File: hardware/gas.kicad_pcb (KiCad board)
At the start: 2 copper layers, 65 x 30 mm, 24 parts, among them P1 CON-SENSOR2, P2 DEBUG, P3 BOOT, P4 Gas Sensor, U1 XMC1300, U2 DRILL, U3 DRILL, U4 DRILL, U5 DRILL

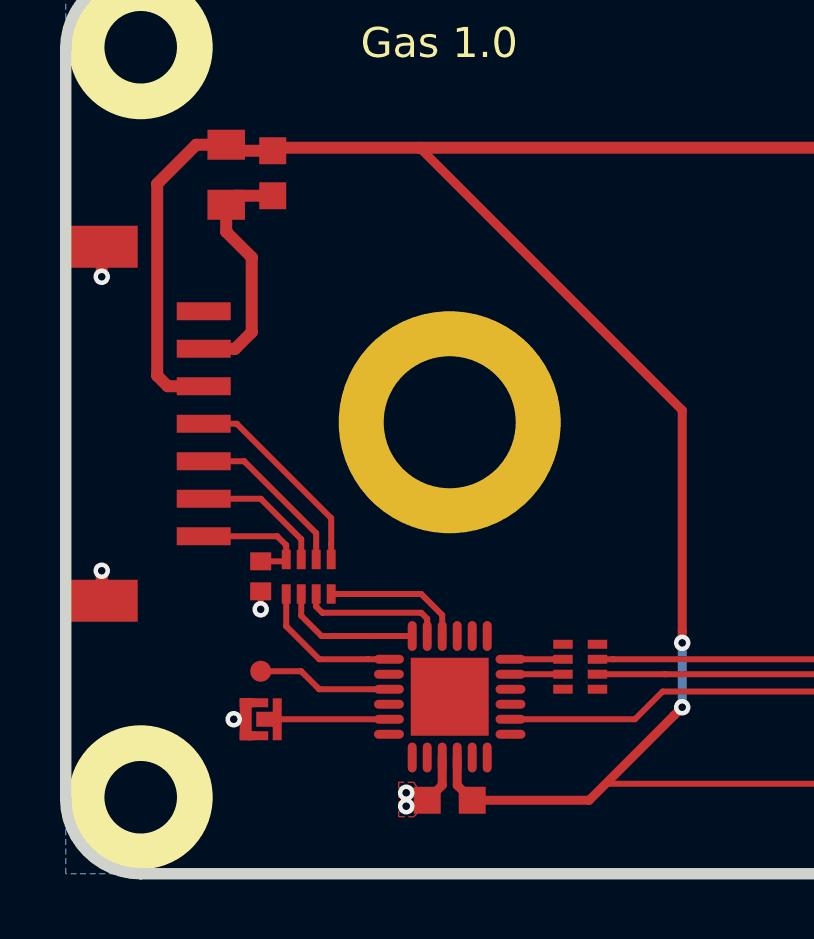
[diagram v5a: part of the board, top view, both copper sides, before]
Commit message: updated M3 spacer footprint, drc check
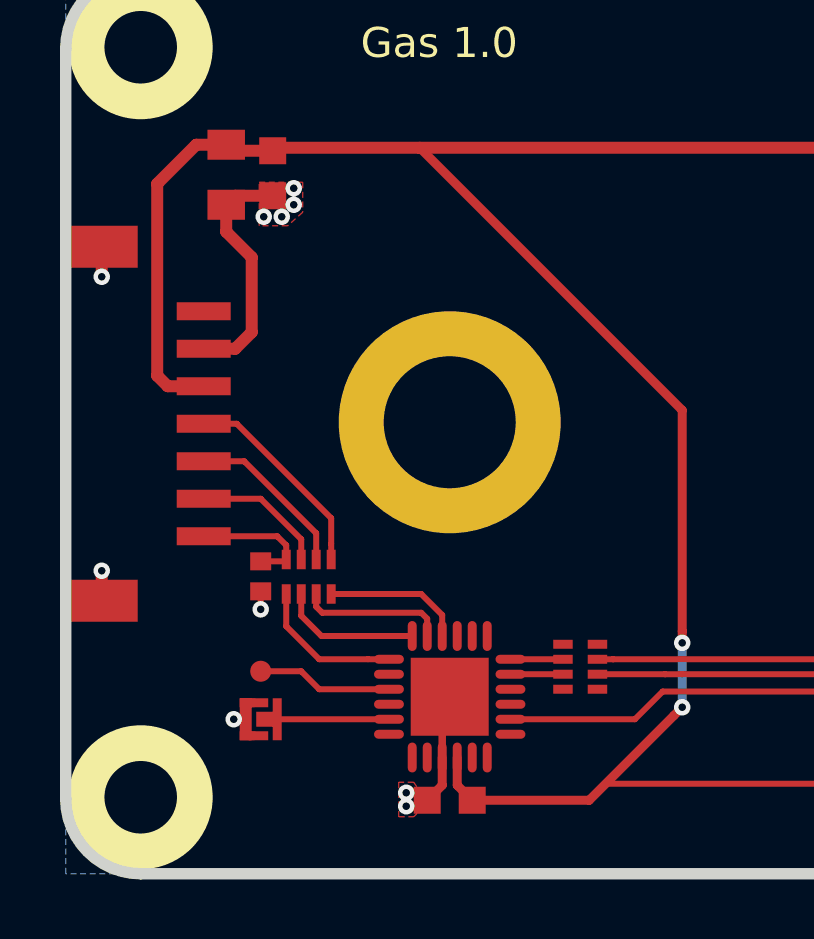
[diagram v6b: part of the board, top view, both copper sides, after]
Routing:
- net GND: track 25.9 -> 31.4 mm, vias 8 -> 12
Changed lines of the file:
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@@
-(kicad_pcb (version 20171130) (host pcbnew 5.0.2-bee76a0~70~ubuntu18.04.1)
+(kicad_pcb (version 20171130) (host pcbnew 5.0.2-bee76a0~70~ubuntu18.10.1)
   (general
     (thickness 1.6)
     (drawings 15)
-    (tracks 137)
+    (tracks 146)
     (zones 0)
     (modules 24)
@@
   )
   (setup
-    (last_trace_width 0.2)
+    (last_trace_width 0.4)
     (user_trace_width 0.2)
     (user_trace_width 0.3)
@@
       (effects (font (size 0.3 0.3) (thickness 0.05)))
     )
-    (pad "" thru_hole circle (at 0 0) (size 7.4 7.4) (drill 4.4) (layers *.Cu *.Mask F.Paste))
+    (fp_poly (pts (xy 2.12 0.61) (xy 2.23 0.15) (xy 3.71 0.15) (xy 3.54 1.08)) (layer F.Paste) (width 0))
+    (fp_poly (pts (xy -0.665 2.11) (xy -0.15 2.2) (xy -0.15 3.68) (xy -1.19 3.49)) (layer F.Paste) (width 0))
+    (fp_poly (pts (xy -2.12 -0.62) (xy -2.2 -0.15) (xy -3.68 -0.15) (xy -3.48 -1.23)) (layer F.Paste) (width 0))
+    (fp_poly (pts (xy 0.63 -2.12) (xy 0.15 -2.2) (xy 0.15 -3.68) (xy 1.24 -3.48)) (layer F.Paste) (width 0))
+    (fp_arc (start 0 0) (end 2.8 -0.9) (angle -51.9) (layer F.Paste) (width 1.5))
+    (fp_arc (start 0 0) (end -0.9 -2.8) (angle -51.9) (layer F.Paste) (width 1.5))
+    (fp_arc (start 0 0) (end 0.94 2.8) (angle -53.57730467) (layer F.Paste) (width 1.5))
+    (fp_arc (start 0 0) (end -2.8 0.9) (angle -51.9) (layer F.Paste) (width 1.5))
+    (fp_poly (pts (xy -1.04 -3.54) (xy -0.15 -3.68) (xy -0.15 -2.2) (xy -0.59 -2.12)) (layer F.Paste) (width 0))
+    (fp_poly (pts (xy 1.12 3.53) (xy 0.15 3.68) (xy 0.15 2.2) (xy 0.68 2.1)) (layer F.Paste) (width 0))
+    (fp_poly (pts (xy 3.55 -1.03) (xy 3.69 -0.15) (xy 2.21 -0.15) (xy 2.13 -0.58)) (layer F.Paste) (width 0))
+    (fp_poly (pts (xy -3.54 1.01) (xy -3.68 0.15) (xy -2.2 0.15) (xy -2.1 0.64)) (layer F.Paste) (width 0))
+    (pad "" thru_hole circle (at 0 0) (size 7.4 7.4) (drill 4.4) (layers *.Cu *.Mask))
   )
   (module kicad-libraries:pin_array_8x1_smd (layer F.Cu)
@@
       (xy -0.55372 -1.41224) (xy -0.55372 -1.67132)) (layer B.SilkS) (width 0.00254))
   )
+  (gr_line (start 127.7 105.3) (end 127.7 84.5) (layer F.Fab) (width 0.2))
   (gr_text "Gas 1.0" (at 132.45 82.31) (layer F.SilkS)
     (effects (font (size 1 1) (thickness 0.15)))
@@
   )
   (gr_line (start 127.7 84.5) (end 172.2 84.5) (layer F.Fab) (width 0.2))
-  (gr_line (start 127.7 105.3) (end 127.7 84.5) (layer F.Fab) (width 0.2))
   (gr_line (start 172.2 105.3) (end 127.7 105.3) (layer F.Fab) (width 0.2))
   (gr_line (start 172.2 84.5) (end 172.2 105.3) (layer F.Fab) (width 0.2))
@@
   (segment (start 125.65076 87.4) (end 125.35 87.70076) (width 0.4) (layer F.Cu) (net 2))
   (segment (start 126.9 87.4) (end 125.65076 87.4) (width 0.4) (layer F.Cu) (net 2))
-  (segment (start 125.35 88.60114) (end 125.35 87.70076) (width 0.4) (layer F.Cu) (net 2))
-  (segment (start 126.2 91.95) (end 126.2 89.45114) (width 0.4) (layer F.Cu) (net 2))
-  (segment (start 124.6 92.5) (end 125.65 92.5) (width 0.4) (layer F.Cu) (net 2))
-  (segment (start 126.2 89.45114) (end 125.35 88.60114) (width 0.4) (layer F.Cu) (net 2))
-  (segment (start 125.65 92.5) (end 126.2 91.95) (width 0.4) (layer F.Cu) (net 2))
   (via (at 121.2 90.1) (size 0.55) (drill 0.25) (layers F.Cu B.Cu) (net 2))
   (segment (start 121.2 89.1) (end 121.2 90.1) (width 0.4) (layer F.Cu) (net 2))
@@
   (via (at 125.6 104.85) (size 0.55) (drill 0.25) (layers F.Cu B.Cu) (net 2))
   (segment (start 126 104.85) (end 125.6 104.85) (width 0.3) (layer F.Cu) (net 2))
+  (segment (start 132.55 105.15) (end 132.15 104.75) (width 0.25) (layer F.Cu) (net 2))
+  (segment (start 132.55 106.125) (end 132.55 105.15) (width 0.25) (layer F.Cu) (net 2))
+  (segment (start 132.15 104.75) (end 132.15 103.45) (width 0.25) (layer F.Cu) (net 2))
+  (segment (start 132.15 103.45) (end 133.45 103.45) (width 0.25) (layer F.Cu) (net 2))
+  (segment (start 133.45 103.45) (end 133.45 104.75) (width 0.25) (layer F.Cu) (net 2))
+  (segment (start 125.35 88.60114) (end 125.35 87.70076) (width 0.4) (layer F.Cu) (net 2))
+  (segment (start 126.2 89.45114) (end 125.35 88.60114) (width 0.4) (layer F.Cu) (net 2))
+  (segment (start 126.2 91.95) (end 126.2 89.45114) (width 0.4) (layer F.Cu) (net 2))
+  (segment (start 124.6 92.5) (end 125.65 92.5) (width 0.4) (layer F.Cu) (net 2))
+  (segment (start 125.65 92.5) (end 126.2 91.95) (width 0.4) (layer F.Cu) (net 2))
+  (via (at 126.6 88.1) (size 0.55) (drill 0.25) (layers F.Cu B.Cu) (net 2))
+  (via (at 127.2 88.1) (size 0.55) (drill 0.25) (layers F.Cu B.Cu) (net 2))
+  (via (at 127.6 87.15) (size 0.55) (drill 0.25) (layers F.Cu B.Cu) (net 2))
+  (via (at 127.6 87.7) (size 0.55) (drill 0.25) (layers F.Cu B.Cu) (net 2))
   (segment (start 125.0993 95) (end 124.6 95) (width 0.2) (layer F.Cu) (net 3))
   (segment (start 128.8493 99) (end 128.8493 99.525) (width 0.2) (layer F.Cu) (net 3))
@@
       )
     )
+  )
+  (zone (net 2) (net_name GND) (layer F.Cu) (hatch edge 0.508)
+    (connect_pads yes (clearance 0.1))
+    (min_thickness 0.1)
+    (fill yes (arc_segments 16) (thermal_gap 0.508) (thermal_bridge_width 0.508))
+    (polygon
+      (pts
+        (xy 126.45 86.95) (xy 127.9 86.95) (xy 127.9 87.95) (xy 127.4 88.4) (xy 126.45 88.4)
+        (xy 126.45 87.85)
+      )
+    )

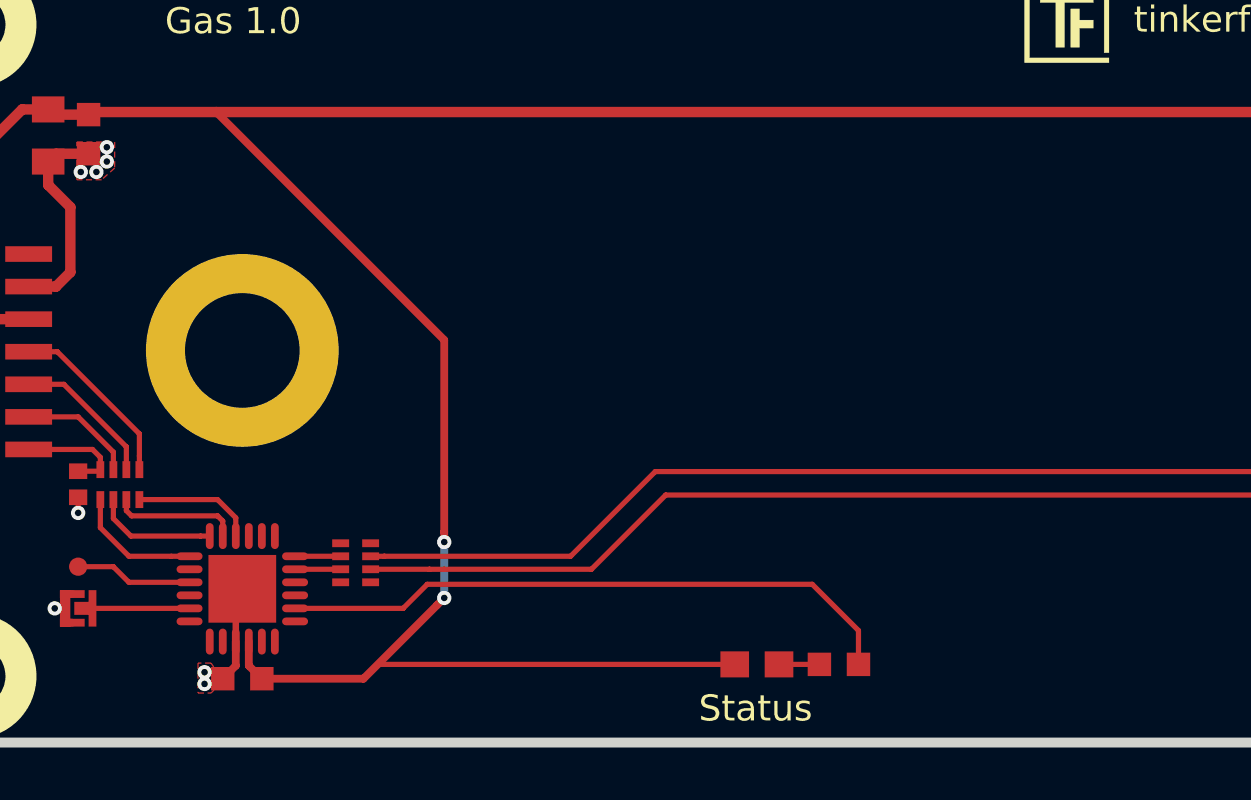
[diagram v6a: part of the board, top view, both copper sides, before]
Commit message: changed status led placement, plotted gerber files
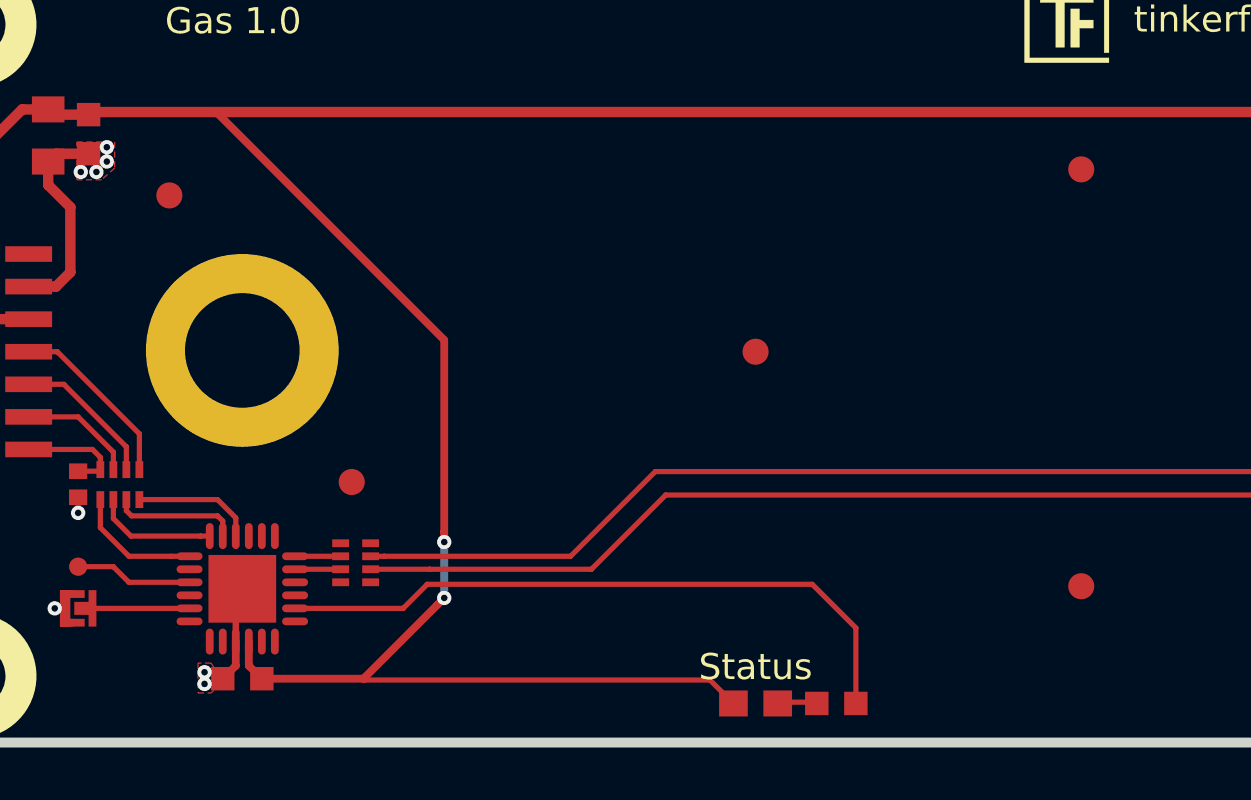
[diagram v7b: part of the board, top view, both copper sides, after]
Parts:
- added Fiducial_Mark: VAL**, kicad-libraries:Fiducial_Mark, F.Cu at (130.0, 89.0)
- added Fiducial_Mark: VAL**, kicad-libraries:Fiducial_Mark, F.Cu at (152.5, 95.0)
- added Fiducial_Mark: VAL**, kicad-libraries:Fiducial_Mark, F.Cu at (165.0, 88.0)
- added Fiducial_Mark: VAL**, kicad-libraries:Fiducial_Mark, F.Cu at (165.0, 104.0)
- added Fiducial_Mark: VAL**, kicad-libraries:Fiducial_Mark, F.Cu at (137.0, 100.0)
- moved R1 1.50 mm to (155.6, 108.5)
- moved D1 1.50 mm to (152.5, 108.5)
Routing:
- net Net-(R1-Pad1): track 24.0 -> 25.5 mm
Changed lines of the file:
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@@
     (thickness 1.6)
     (drawings 15)
-    (tracks 146)
+    (tracks 147)
     (zones 0)
-    (modules 24)
+    (modules 29)
     (nets 41)
   )
@@
   )
   (setup
-    (last_trace_width 0.4)
+    (last_trace_width 0.25)
     (user_trace_width 0.2)
     (user_trace_width 0.3)
@@
     (pad_drill 0.6)
     (pad_to_mask_clearance 0)
-    (solder_mask_min_width 0.25)
     (aux_axis_origin 120 80)
     (grid_origin 120 80)
@@
     (pcbplotparams
       (layerselection 0x010fc_ffffffff)
-      (usegerberextensions false)
+      (usegerberextensions true)
       (usegerberattributes false)
       (usegerberadvancedattributes false)
@@
       (outputformat 1)
       (mirror false)
-      (drillshape 1)
+      (drillshape 0)
       (scaleselection 1)
-      (outputdirectory ""))
+      (outputdirectory "proto/"))
   )
   (net 0 "")
@@
   )
   (module kicad-libraries:R0603F (layer F.Cu)
-    (at 155.7 107 180)
+    (at 155.6 108.5 180)
     (attr smd)
     (fp_text reference R1 (at 0.05 0.225) (layer F.Fab)
@@
   )
   (module kicad-libraries:D0603E (layer F.Cu)
-    (at 152.55 107)
+    (at 152.5 108.5)
     (attr smd)
     (fp_text reference D1 (at 0.85 0.45) (layer F.Fab)
@@
       (xy -0.55372 -1.41224) (xy -0.55372 -1.67132)) (layer B.SilkS) (width 0.00254))
   )
+  (module kicad-libraries:Fiducial_Mark (layer F.Cu)
+    (at 130 89)
+    (attr smd)
+    (fp_text reference Fiducial_Mark (at 0 0) (layer F.SilkS) hide
+      (effects (font (size 0.127 0.127) (thickness 0.03302)))
+    )
+    (fp_text value VAL** (at 0 -0.29972) (layer F.SilkS) hide
+      (effects (font (size 0.127 0.127) (thickness 0.03302)))
+    )
+    (fp_circle (center 0 0) (end 1.15062 0) (layer Dwgs.User) (width 0.01016))
+    (pad 1 smd circle (at 0 0) (size 1.00076 1.00076) (layers F.Cu F.Paste F.Mask)
+      (clearance 0.65024))
+  )
+  (module kicad-libraries:Fiducial_Mark (layer F.Cu)
+    (at 152.5 95)
+    (attr smd)
+    (fp_text reference Fiducial_Mark (at 0 0) (layer F.SilkS) hide
+      (effects (font (size 0.127 0.127) (thickness 0.03302)))
+    )
+    (fp_text value VAL** (at 0 -0.29972) (layer F.SilkS) hide
+      (effects (font (size 0.127 0.127) (thickness 0.03302)))
+    )
+    (fp_circle (center 0 0) (end 1.15062 0) (layer Dwgs.User) (width 0.01016))
+    (pad 1 smd circle (at 0 0) (size 1.00076 1.00076) (layers F.Cu F.Paste F.Mask)
+      (clearance 0.65024))
+  )
+  (module kicad-libraries:Fiducial_Mark (layer F.Cu)
+    (at 165 88)
+    (attr smd)
+    (fp_text reference Fiducial_Mark (at 0 0) (layer F.SilkS) hide
+      (effects (font (size 0.127 0.127) (thickness 0.03302)))
+    )
+    (fp_text value VAL** (at 0 -0.29972) (layer F.SilkS) hide
+      (effects (font (size 0.127 0.127) (thickness 0.03302)))
+    )
+    (fp_circle (center 0 0) (end 1.15062 0) (layer Dwgs.User) (width 0.01016))
+    (pad 1 smd circle (at 0 0) (size 1.00076 1.00076) (layers F.Cu F.Paste F.Mask)
+      (clearance 0.65024))
+  )
+  (module kicad-libraries:Fiducial_Mark (layer F.Cu)
+    (at 165 104)
+    (attr smd)
+    (fp_text reference Fiducial_Mark (at 0 0) (layer F.SilkS) hide
+      (effects (font (size 0.127 0.127) (thickness 0.03302)))
+    )
+    (fp_text value VAL** (at 0 -0.29972) (layer F.SilkS) hide
+      (effects (font (size 0.127 0.127) (thickness 0.03302)))
+    )
+    (fp_circle (center 0 0) (end 1.15062 0) (layer Dwgs.User) (width 0.01016))
+    (pad 1 smd circle (at 0 0) (size 1.00076 1.00076) (layers F.Cu F.Paste F.Mask)
+      (clearance 0.65024))
+  )
+  (module kicad-libraries:Fiducial_Mark (layer F.Cu)
+    (at 137 100)
+    (attr smd)
+    (fp_text reference Fiducial_Mark (at 0 0) (layer F.SilkS) hide
+      (effects (font (size 0.127 0.127) (thickness 0.03302)))
+    )
+    (fp_text value VAL** (at 0 -0.29972) (layer F.SilkS) hide
+      (effects (font (size 0.127 0.127) (thickness 0.03302)))
+    )
+    (fp_circle (center 0 0) (end 1.15062 0) (layer Dwgs.User) (width 0.01016))
+    (pad 1 smd circle (at 0 0) (size 1.00076 1.00076) (layers F.Cu F.Paste F.Mask)
+      (clearance 0.65024))
+  )
   (gr_line (start 127.7 105.3) (end 127.7 84.5) (layer F.Fab) (width 0.2))
   (gr_text "Gas 1.0" (at 132.45 82.31) (layer F.SilkS)
@@
     (effects (font (size 1 1) (thickness 0.15)))
   )
-  (gr_text Status (at 152.5 108.69) (layer F.SilkS)
+  (gr_text Status (at 152.5 107.1) (layer F.SilkS)
     (effects (font (size 1 1) (thickness 0.15)))
   )
@@
   (segment (start 137.450009 107.55) (end 140.275001 104.725008) (width 0.3) (layer F.Cu) (net 1))
   (segment (start 140.55 102.303968) (end 140.55 104.450009) (width 0.3) (layer B.Cu) (net 1))
-  (segment (start 138.000009 107) (end 151.6999 107) (width 0.2) (layer F.Cu) (net 1))
-  (segment (start 137.450009 107.55) (end 138.000009 107) (width 0.2) (layer F.Cu) (net 1))
+  (segment (start 150.7499 107.6) (end 151.6499 108.5) (width 0.2) (layer F.Cu) (net 1))
+  (segment (start 137.450009 107.55) (end 137.500009 107.6) (width 0.2) (layer F.Cu) (net 1))
+  (segment (start 137.500009 107.6) (end 150.7499 107.6) (width 0.2) (layer F.Cu) (net 1))
   (segment (start 183.04924 89.35076) (end 183.25 89.15) (width 0.4) (layer F.Cu) (net 2))
   (segment (start 181.75 89.35076) (end 183.04924 89.35076) (width 0.4) (layer F.Cu) (net 2))
@@
   (segment (start 138.25108 102.85) (end 145.4 102.85) (width 0.2) (layer F.Cu) (net 7))
   (segment (start 145.4 102.85) (end 148.65 99.6) (width 0.2) (layer F.Cu) (net 7))
-  (segment (start 156.45 105.7) (end 156.45 107) (width 0.2) (layer F.Cu) (net 8))
-  (segment (start 154.675999 103.925999) (end 156.45 105.7) (width 0.2) (layer F.Cu) (net 8))
+  (segment (start 156.35 105.6) (end 156.35 108.5) (width 0.2) (layer F.Cu) (net 8))
+  (segment (start 154.675999 103.925999) (end 156.35 105.6) (width 0.2) (layer F.Cu) (net 8))
   (segment (start 139.898479 103.925999) (end 154.675999 103.925999) (width 0.2) (layer F.Cu) (net 8))
   (segment (start 134.825 104.85) (end 138.974478 104.85) (width 0.2) (layer F.Cu) (net 8))
@@
   (segment (start 124.6 98.75) (end 127.05 98.75) (width 0.2) (layer F.Cu) (net 15))
   (segment (start 127.05 98.75) (end 127.3507 99.0507) (width 0.2) (layer F.Cu) (net 15))
-  (segment (start 153.4001 107) (end 154.95 107) (width 0.2) (layer F.Cu) (net 16))
+  (segment (start 153.3 108.45) (end 154.8499 108.45) (width 0.2) (layer F.Cu) (net 16))
   (segment (start 127.85 103.25) (end 126.5 103.25) (width 0.2) (layer F.Cu) (net 18))
   (segment (start 130.775 103.85) (end 128.45 103.85) (width 0.2) (layer F.Cu) (net 18))
